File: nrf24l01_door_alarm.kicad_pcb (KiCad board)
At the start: 2 copper layers, 26.2 x 45.7 mm, 17 parts, among them J1 Conn_01x02_Male, J2 Conn_02x03_Odd_Even, Q1 2N7002, SW1 SW_Reed, U1 ATmega328P-AU, U2 NRF24L01_Breakout

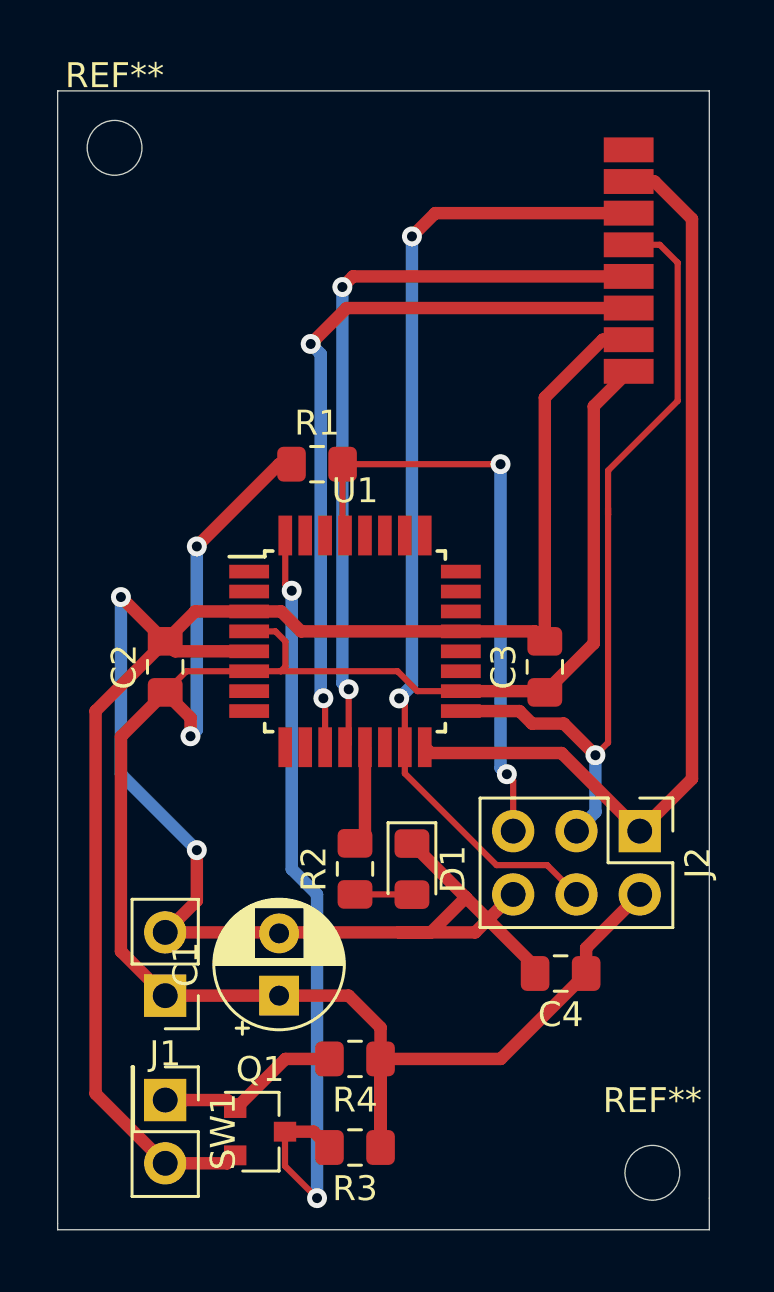
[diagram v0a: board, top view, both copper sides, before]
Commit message: compact pcb layout
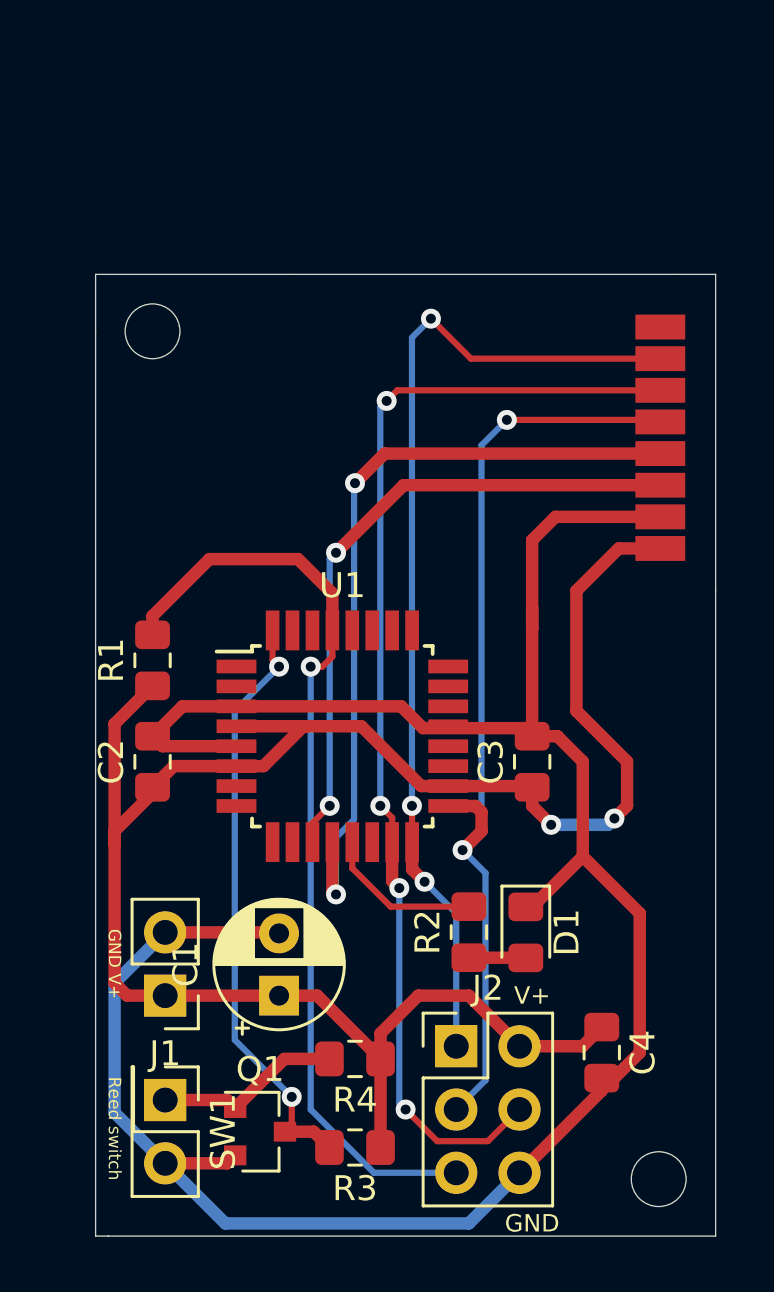
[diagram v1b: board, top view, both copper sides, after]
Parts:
-  : renamed from REF** (x2)
- moved J2 11.4 mm to (171.2, 119.1), turned to 0 degrees
- moved R1 10.3 mm to (159.0, 103.6), turned to 90 degrees
- moved   7.52 mm to (159.0, 90.4)
- moved U2 7.22 mm to (170.7, 94.7)
- moved D1 5.23 mm to (174.0, 114.6)
- moved R2 5.23 mm to (171.7, 114.5)
- moved C2 3.84 mm to (159.0, 107.7)
- moved C3 3.84 mm to (174.2, 107.7)
- moved U1 3.84 mm to (166.6, 106.7)
- moved C4 3.58 mm to (177.0, 119.4), turned to 270 degrees
- moved   0.36 mm to (179.3, 124.5)
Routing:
- net GND: track 118.3 -> 93.9 mm, vias 2 -> 0
- net Vcc: track 101.8 -> 81.5 mm
- net RESET: track 24.2 -> 37.7 mm, vias 2 -> 1
- net EXT_INTERRUPT: track 32.4 -> 24.1 mm
- net MOSI: track 39.9 -> 45.8 mm, vias 2 -> 4
- net SCK: track 33.2 -> 38.8 mm, vias 1 -> 2
- net CE: track 29.8 -> 26.1 mm
- net INTERRUPT_INDICATOR: track 4.03 -> 6.37 mm
- net MISO: track 38.6 -> 40.1 mm, vias 0 -> 3
- net CSN: track 30.3 -> 31.7 mm
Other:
- board size 26.2 x 45.7 mm -> 24.9 x 38.6 mm
- board text added: "GND"
- board text added: "GND V+"
- board text added: "Reed switch"
- board text added: "V+"
- board text added: "nrf24l01 door alarm v0.1 Yovan Naumovski - 2020"
